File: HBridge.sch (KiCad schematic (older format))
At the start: 27 parts, among them Q1 RTQ020N03, Q2 RTQ020N03, Q3 RTQ020N03, Q4 RTQ020N03

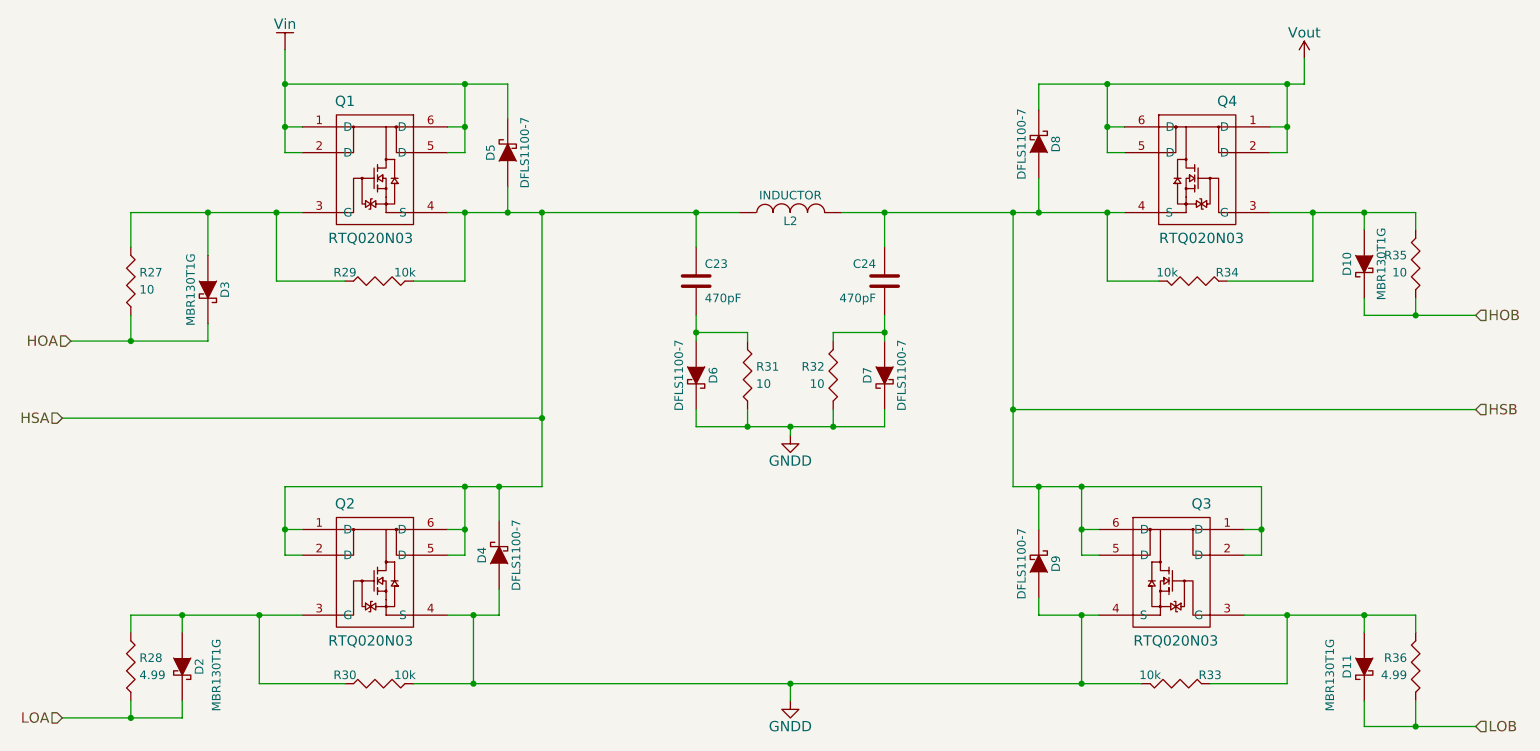
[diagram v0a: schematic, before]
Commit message: Started placing components
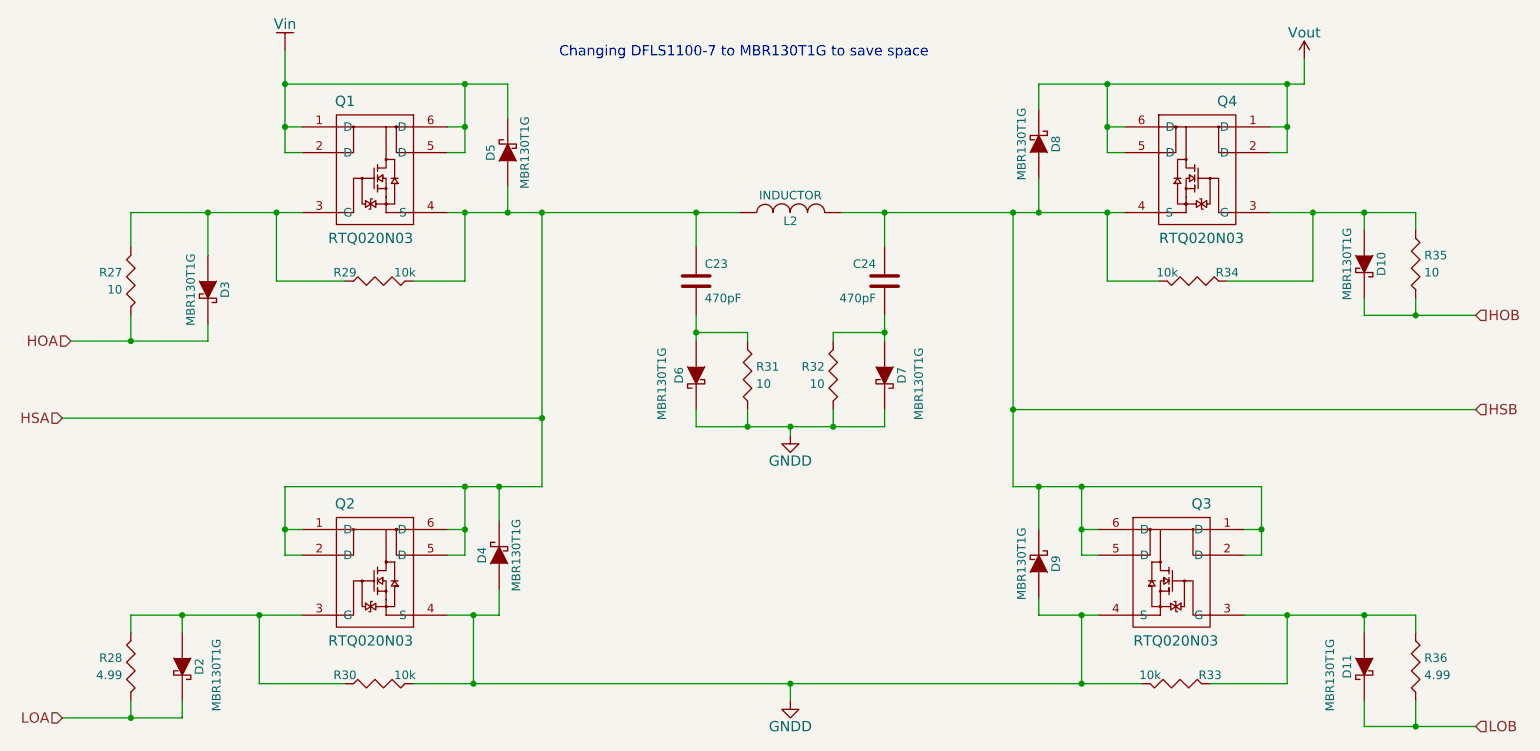
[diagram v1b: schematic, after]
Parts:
- D10, D11, D2, D3: footprint Diodes_SMD:Diode-SMA_Handsoldering -> KiCadFP:Diode-SOD_123_Handsoldering
- D4, D5, D6, D7, D8, D9: value DFLS1100-7 -> MBR130T1G; footprint Diodes_SMD:Diode-SMA_Handsoldering -> KiCadFP:Diode-SOD_123_Handsoldering; PN DFLS1100-7 -> MBR130T1G
- Q1, Q2, Q3, Q4: footprint Housings_SOT-23_SOT-143_TSOT-6:SOT23-6 -> Housings_SOT-23_SOT-143_TSOT-6:TSOT-6-MK06A_Handsoldering
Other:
- note added: "Changing DFLS1100-7 to MBR130T1G to save space"
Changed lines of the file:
@@
 LIBS:valves
 LIBS:SelfGenerated
+LIBS:ipc-7351-diode
 LIBS:Project_2-cache
 EELAYER 25 0
@@
 F 0 "Q1" V 3300 1550 60  0000 C CNN
 F 1 "RTQ020N03" V 4100 1700 60  0000 C CNN
-F 2 "Housings_SOT-23_SOT-143_TSOT-6:SOT23-6" H 3700 1750 60  0001 C CNN
+F 2 "Housings_SOT-23_SOT-143_TSOT-6:TSOT-6-MK06A_Handsoldering" H 3700 1750 60  0001 C CNN
 F 3 "" H 3700 1750 60  0000 C CNN
 	1    3700 1750
@@
 $EndComp
 $Comp
-L Vin #PWR053
+L Vin #PWR051
 U 1 1 54F15F11
 P 3150 1050
-F 0 "#PWR053" H 3150 900 60  0001 C CNN
+F 0 "#PWR051" H 3150 900 60  0001 C CNN
 F 1 "Vin" H 3150 1200 60  0000 C CNN
 F 2 "" H 3150 1050 60  0000 C CNN
@@
 F 3 "" H 2250 2400 30  0000 C CNN
 	1    2250 2400
-	1    0    0    -1
+	-1   0    0    -1
 $EndComp
 $Comp
@@
 F 0 "D3" H 2700 2550 50  0000 C CNN
 F 1 "MBR130T1G" H 2700 2350 50  0000 C CNN
-F 2 "Diodes_SMD:Diode-SMA_Handsoldering" H 2700 2450 60  0001 C CNN
+F 2 "KiCadFP:Diode-SOD_123_Handsoldering" H 2700 2450 60  0001 C CNN
 F 3 "" H 2700 2450 60  0000 C CNN
 F 4 "MBR130T1G" H 2700 2450 60  0001 C CNN "PN"
@@
 $EndComp
 $Comp
-L DIODESCH D5
-U 1 1 54F16C43
-P 4450 1650
-F 0 "D5" H 4450 1750 50  0000 C CNN
-F 1 "DFLS1100-7" H 4450 1550 50  0000 C CNN
-F 2 "Diodes_SMD:Diode-SMA_Handsoldering" H 4450 1650 60  0001 C CNN
-F 3 "" H 4450 1650 60  0000 C CNN
-F 4 "DFLS1100-7" H 4450 1650 60  0001 C CNN "PN"
-	1    4450 1650
-	0    -1   -1   0
-$EndComp
-$Comp
 L Rv R28
 U 1 1 54F17237
@@
 F 3 "" H 2250 4650 30  0000 C CNN
 	1    2250 4650
-	1    0    0    -1
+	-1   0    0    -1
 $EndComp
 $Comp
@@
 F 0 "D2" H 2550 4750 50  0000 C CNN
 F 1 "MBR130T1G" H 2600 4850 50  0000 C CNN
-F 2 "Diodes_SMD:Diode-SMA_Handsoldering" H 2550 4650 60  0001 C CNN
+F 2 "KiCadFP:Diode-SOD_123_Handsoldering" H 2550 4650 60  0001 C CNN
 F 3 "" H 2550 4650 60  0000 C CNN
 F 4 "MBR130T1G" H 2550 4650 60  0001 C CNN "PN"
@@
 F 0 "Q2" V 3300 3900 60  0000 C CNN
 F 1 "RTQ020N03" V 4100 4050 60  0000 C CNN
-F 2 "Housings_SOT-23_SOT-143_TSOT-6:SOT23-6" H 3700 4100 60  0001 C CNN
+F 2 "Housings_SOT-23_SOT-143_TSOT-6:TSOT-6-MK06A_Handsoldering" H 3700 4100 60  0001 C CNN
 F 3 "" H 3700 4100 60  0000 C CNN
 	1    3700 4100
 	0    1    1    0
-$EndComp
-$Comp
-L DIODESCH D4
-U 1 1 54F1760B
-P 4400 4000
-F 0 "D4" H 4400 4100 50  0000 C CNN
-F 1 "DFLS1100-7" H 4400 3900 50  0000 C CNN
-F 2 "Diodes_SMD:Diode-SMA_Handsoldering" H 4400 4000 60  0001 C CNN
-F 3 "" H 4400 4000 60  0000 C CNN
-F 4 "DFLS1100-7" H 4400 4000 60  0001 C CNN "PN"
-	1    4400 4000
-	0    -1   -1   0
 $EndComp
 $Comp
@@
 $EndComp
 $Comp
-L DIODESCH D6
-U 1 1 54F1B1EB
-P 5550 2950
-F 0 "D6" H 5550 3050 50  0000 C CNN
-F 1 "DFLS1100-7" H 5550 2850 50  0000 C CNN
-F 2 "Diodes_SMD:Diode-SMA_Handsoldering" H 5550 2950 60  0001 C CNN
-F 3 "" H 5550 2950 60  0000 C CNN
-F 4 "DFLS1100-7" H 5550 2950 60  0001 C CNN "PN"
-	1    5550 2950
-	0    1    1    0
-$EndComp
-$Comp
 L Rv R31
 U 1 1 54F1B288
@@
 F 0 "Q4" V 8050 1550 60  0000 C CNN
 F 1 "RTQ020N03" V 8850 1700 60  0000 C CNN
-F 2 "Housings_SOT-23_SOT-143_TSOT-6:SOT23-6" H 8450 1750 60  0001 C CNN
+F 2 "Housings_SOT-23_SOT-143_TSOT-6:TSOT-6-MK06A_Handsoldering" H 8450 1750 60  0001 C CNN
 F 3 "" H 8450 1750 60  0000 C CNN
 	1    8450 1750
@@
 F 3 "" H 9750 2300 30  0000 C CNN
 	1    9750 2300
-	-1   0    0    -1
+	1    0    0    -1
 $EndComp
 $Comp
@@
 F 0 "D10" H 9450 2400 50  0000 C CNN
 F 1 "MBR130T1G" H 9450 2200 50  0000 C CNN
-F 2 "Diodes_SMD:Diode-SMA_Handsoldering" H 9450 2300 60  0001 C CNN
+F 2 "KiCadFP:Diode-SOD_123_Handsoldering" H 9450 2300 60  0001 C CNN
 F 3 "" H 9450 2300 60  0000 C CNN
 F 4 "MBR130T1G" H 9450 2300 60  0001 C CNN "PN"
 	1    9450 2300
-	0    -1   1    0
+	0    1    1    0
 $EndComp
 $Comp
@@
 $EndComp
 $Comp
-L DIODESCH D8
-U 1 1 54F1CF31
-P 7550 1600
-F 0 "D8" H 7550 1700 50  0000 C CNN
-F 1 "DFLS1100-7" H 7550 1500 50  0000 C CNN
-F 2 "Diodes_SMD:Diode-SMA_Handsoldering" H 7550 1600 60  0001 C CNN
-F 3 "" H 7550 1600 60  0000 C CNN
-F 4 "DFLS1100-7" H 7550 1600 60  0001 C CNN "PN"
-	1    7550 1600
-	0    1    -1   0
-$EndComp
-$Comp
 L Rv R36
 U 1 1 54F1CF37
@@
 F 3 "" H 9750 4650 30  0000 C CNN
 	1    9750 4650
-	-1   0    0    -1
+	1    0    0    -1
 $EndComp
 $Comp
@@
 F 0 "D11" H 9450 4750 50  0000 C CNN
 F 1 "MBR130T1G" H 9500 4850 50  0000 C CNN
-F 2 "Diodes_SMD:Diode-SMA_Handsoldering" H 9450 4650 60  0001 C CNN
+F 2 "KiCadFP:Diode-SOD_123_Handsoldering" H 9450 4650 60  0001 C CNN
 F 3 "" H 9450 4650 60  0000 C CNN
 F 4 "MBR130T1G" H 9450 4650 60  0001 C CNN "PN"
@@
 F 0 "Q3" V 7900 3900 60  0000 C CNN
 F 1 "RTQ020N03" V 8700 4050 60  0000 C CNN
-F 2 "Housings_SOT-23_SOT-143_TSOT-6:SOT23-6" H 8300 4100 60  0001 C CNN
+F 2 "Housings_SOT-23_SOT-143_TSOT-6:TSOT-6-MK06A_Handsoldering" H 8300 4100 60  0001 C CNN
 F 3 "" H 8300 4100 60  0000 C CNN
 	1    8300 4100
 	0    -1   1    0
-$EndComp
-$Comp
-L DIODESCH D9
-U 1 1 54F1CF4B
-P 7550 4050
-F 0 "D9" H 7550 4150 50  0000 C CNN
-F 1 "DFLS1100-7" H 7550 3950 50  0000 C CNN
-F 2 "Diodes_SMD:Diode-SMA_Handsoldering" H 7550 4050 60  0001 C CNN
-F 3 "" H 7550 4050 60  0000 C CNN
-F 4 "DFLS1100-7" H 7550 4050 60  0001 C CNN "PN"
-	1    7550 4050
-	0    1    -1   0
 $EndComp
 $Comp
@@
 $EndComp
 $Comp
-L DIODESCH D7
-U 1 1 54F1CF91
-P 6650 2950
-F 0 "D7" H 6650 3050 50  0000 C CNN
-F 1 "DFLS1100-7" H 6650 2850 50  0000 C CNN
-F 2 "Diodes_SMD:Diode-SMA_Handsoldering" H 6650 2950 60  0001 C CNN
-F 3 "" H 6650 2950 60  0000 C CNN
-F 4 "DFLS1100-7" H 6650 2950 60  0001 C CNN "PN"
-	1    6650 2950
-	0    -1   1    0
-$EndComp
-$Comp
 L Rv R32
 U 1 1 54F1CF97
@@
 $EndComp
 $Comp
-L GNDD #PWR054
+L GNDD #PWR052
 U 1 1 54F229CA
 P 6100 3300
-F 0 "#PWR054" H 6100 3050 60  0001 C CNN
+F 0 "#PWR052" H 6100 3050 60  0001 C CNN
 F 1 "GNDD" H 6100 3150 60  0000 C CNN
 F 2 "" H 6100 3300 60  0000 C CNN
@@
 $EndComp
 $Comp
-L Vout #PWR055
+L Vout #PWR053
 U 1 1 54F24EF6
 P 9100 1100
-F 0 "#PWR055" H 9100 950 60  0001 C CNN
+F 0 "#PWR053" H 9100 950 60  0001 C CNN
 F 1 "Vout" H 9100 1250 60  0000 C CNN
 F 2 "" H 9100 1100 60  0000 C CNN
@@
 Connection ~ 2700 2000
 $Comp
-L GNDD #PWR056
+L GNDD #PWR054
 U 1 1 54F243ED
 P 6100 4850
-F 0 "#PWR056" H 6100 4600 60  0001 C CNN
+F 0 "#PWR054" H 6100 4600 60  0001 C CNN
 F 1 "GNDD" H 6100 4700 60  0000 C CNN
 F 2 "" H 6100 4850 60  0000 C CNN
@@
 Connection ~ 6100 4750
 Connection ~ 7800 4750
+Text Notes 4750 1100 0    60   ~ 0
+Changing DFLS1100-7 to MBR130T1G to save space
+$Comp
+L DIODESCH D5
+U 1 1 54FDD309
+P 4450 1650
+F 0 "D5" H 4450 1750 50  0000 C CNN
+F 1 "MBR130T1G" H 4450 1550 50  0000 C CNN
+F 2 "KiCadFP:Diode-SOD_123_Handsoldering" H 4450 1650 60  0001 C CNN
+F 3 "" H 4450 1650 60  0000 C CNN
+F 4 "MBR130T1G" H 4450 1650 60  0001 C CNN "PN"
+	1    4450 1650
+	0    -1   -1   0
+$EndComp
+$Comp
+L DIODESCH D8
+U 1 1 54FDD344
+P 7550 1600
+F 0 "D8" H 7550 1700 50  0000 C CNN
+F 1 "MBR130T1G" H 7550 1500 50  0000 C CNN
+F 2 "KiCadFP:Diode-SOD_123_Handsoldering" H 7550 1600 60  0001 C CNN
+F 3 "" H 7550 1600 60  0000 C CNN
+F 4 "MBR130T1G" H 7550 1600 60  0001 C CNN "PN"
+	1    7550 1600
+	0    1    -1   0
+$EndComp
+$Comp
+L DIODESCH D9
+U 1 1 54FDD383
+P 7550 4050
+F 0 "D9" H 7550 4150 50  0000 C CNN
+F 1 "MBR130T1G" H 7550 3950 50  0000 C CNN
+F 2 "KiCadFP:Diode-SOD_123_Handsoldering" H 7550 4050 60  0001 C CNN
+F 3 "" H 7550 4050 60  0000 C CNN
+F 4 "MBR130T1G" H 7550 4050 60  0001 C CNN "PN"
+	1    7550 4050
+	0    1    -1   0
+$EndComp
+$Comp
+L DIODESCH D4
+U 1 1 54FDD3C3
+P 4400 4000
+F 0 "D4" H 4400 4100 50  0000 C CNN
+F 1 "MBR130T1G" H 4400 3900 50  0000 C CNN
+F 2 "KiCadFP:Diode-SOD_123_Handsoldering" H 4400 4000 60  0001 C CNN
+F 3 "" H 4400 4000 60  0000 C CNN
+F 4 "MBR130T1G" H 4400 4000 60  0001 C CNN "PN"
+	1    4400 4000
+	0    -1   -1   0
+$EndComp
+$Comp
+L DIODESCH D6
+U 1 1 54FDD554
+P 5550 2950
+F 0 "D6" H 5550 3050 50  0000 C CNN
+F 1 "MBR130T1G" H 5600 3150 50  0000 C CNN
+F 2 "KiCadFP:Diode-SOD_123_Handsoldering" H 5550 2950 60  0001 C CNN
+F 3 "" H 5550 2950 60  0000 C CNN
+F 4 "MBR130T1G" H 5550 2950 60  0001 C CNN "PN"
+	1    5550 2950
+	0    -1   1    0
+$EndComp
+$Comp
+L DIODESCH D7
+U 1 1 54FDD587
+P 6650 2950
+F 0 "D7" H 6650 3050 50  0000 C CNN
+F 1 "MBR130T1G" H 6700 3150 50  0000 C CNN
+F 2 "KiCadFP:Diode-SOD_123_Handsoldering" H 6650 2950 60  0001 C CNN
+F 3 "" H 6650 2950 60  0000 C CNN
+F 4 "MBR130T1G" H 6650 2950 60  0001 C CNN "PN"
+	1    6650 2950
+	0    1    1    0
+$EndComp
 $EndSCHEMATC

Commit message: still trying to get initial placements done.  Still need to fine-tune
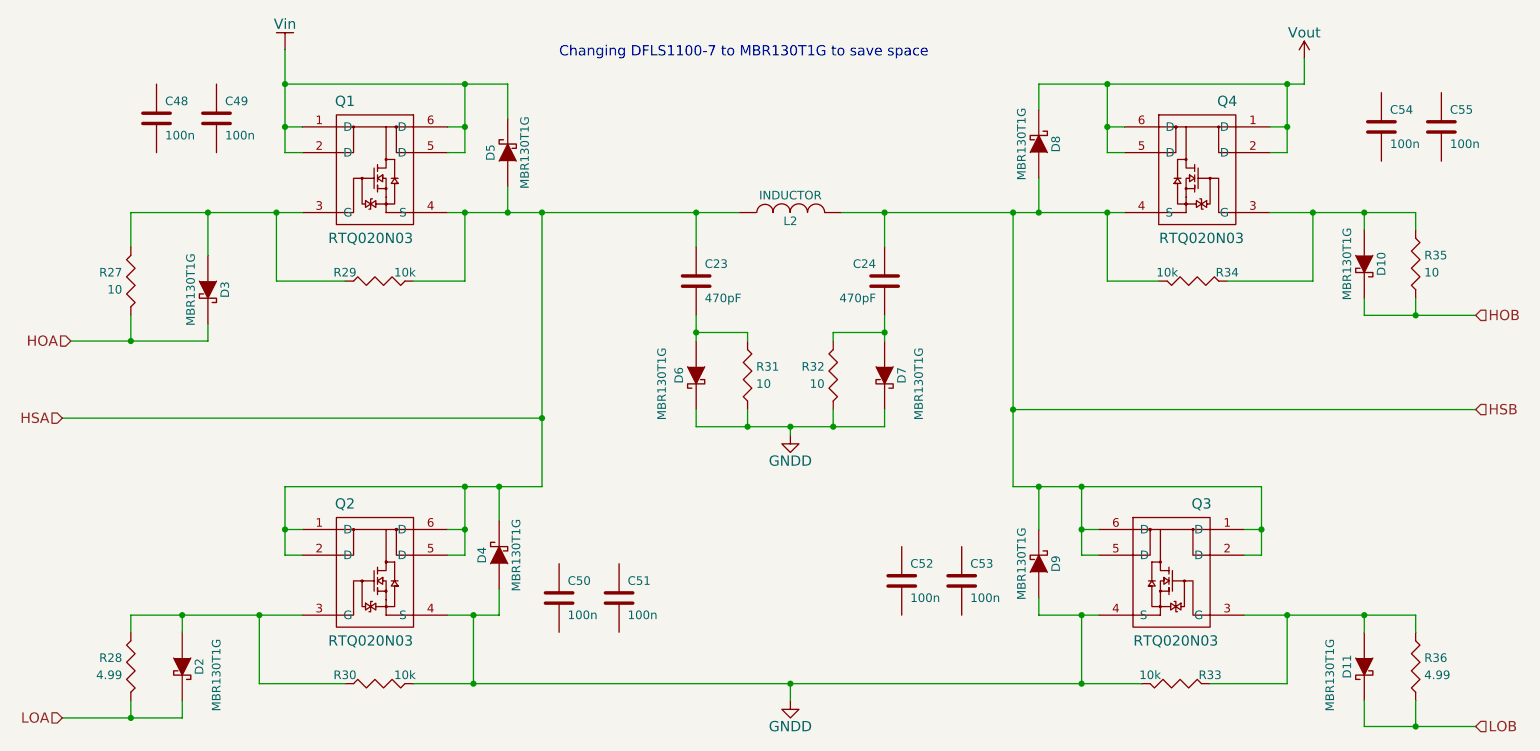
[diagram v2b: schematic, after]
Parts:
- added C48, C49, C50, C51, C52, C53, C54, C55: 100n, symbol C
- C23, C24: footprint Capacitors_SMD:C_0805_HandSoldering -> Capacitors_SMD:C_0603_HandSoldering
- R27, R28, R29, R30, R31, R32, R33, R34, R35, R36: footprint Resistors_SMD:R_0805_HandSoldering -> Resistors_SMD:R_0603_HandSoldering
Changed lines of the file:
@@
 F 0 "R27" H 2300 2450 50  0000 L CNN
 F 1 "10" H 2300 2350 50  0000 L CNN
-F 2 "Resistors_SMD:R_0805_HandSoldering" V 2180 2400 30  0001 C CNN
+F 2 "Resistors_SMD:R_0603_HandSoldering" V 2180 2400 30  0001 C CNN
 F 3 "" H 2250 2400 30  0000 C CNN
 	1    2250 2400
@@
 F 0 "R29" H 3500 2450 50  0000 C CNN
 F 1 "10k" H 3850 2450 50  0000 C CNN
-F 2 "Resistors_SMD:R_0805_HandSoldering" H 3700 2330 30  0001 C CNN
+F 2 "Resistors_SMD:R_0603_HandSoldering" H 3700 2330 30  0001 C CNN
 F 3 "" V 3700 2400 30  0000 C CNN
 	1    3700 2400
@@
 F 0 "R28" H 2300 4700 50  0000 L CNN
 F 1 "4.99" H 2300 4600 50  0000 L CNN
-F 2 "Resistors_SMD:R_0805_HandSoldering" V 2180 4650 30  0001 C CNN
+F 2 "Resistors_SMD:R_0603_HandSoldering" V 2180 4650 30  0001 C CNN
 F 3 "" H 2250 4650 30  0000 C CNN
 	1    2250 4650
@@
 F 0 "R30" H 3500 4800 50  0000 C CNN
 F 1 "10k" H 3850 4800 50  0000 C CNN
-F 2 "Resistors_SMD:R_0805_HandSoldering" H 3700 4680 30  0001 C CNN
+F 2 "Resistors_SMD:R_0603_HandSoldering" H 3700 4680 30  0001 C CNN
 F 3 "" V 3700 4750 30  0000 C CNN
 	1    3700 4750
@@
 F 0 "R31" H 5900 3000 50  0000 L CNN
 F 1 "10" H 5900 2900 50  0000 L CNN
-F 2 "Resistors_SMD:R_0805_HandSoldering" V 5780 2950 30  0001 C CNN
+F 2 "Resistors_SMD:R_0603_HandSoldering" V 5780 2950 30  0001 C CNN
 F 3 "" H 5850 2950 30  0000 C CNN
 	1    5850 2950
@@
 F 0 "C23" H 5600 2500 50  0000 L CNN
 F 1 "470pF" H 5600 2300 50  0000 L CNN
-F 2 "Capacitors_SMD:C_0805_HandSoldering" H 5588 2250 30  0001 C CNN
+F 2 "Capacitors_SMD:C_0603_HandSoldering" H 5588 2250 30  0001 C CNN
 F 3 "" H 5550 2400 60  0000 C CNN
 	1    5550 2400
@@
 F 0 "R35" H 9800 2350 50  0000 L CNN
 F 1 "10" H 9800 2250 50  0000 L CNN
-F 2 "Resistors_SMD:R_0805_HandSoldering" V 9680 2300 30  0001 C CNN
+F 2 "Resistors_SMD:R_0603_HandSoldering" V 9680 2300 30  0001 C CNN
 F 3 "" H 9750 2300 30  0000 C CNN
 	1    9750 2300
@@
 F 0 "R34" H 8250 2450 50  0000 C CNN
 F 1 "10k" H 8600 2450 50  0000 C CNN
-F 2 "Resistors_SMD:R_0805_HandSoldering" H 8450 2330 30  0001 C CNN
+F 2 "Resistors_SMD:R_0603_HandSoldering" H 8450 2330 30  0001 C CNN
 F 3 "" V 8450 2400 30  0000 C CNN
 	1    8450 2400
@@
 F 0 "R36" H 9800 4700 50  0000 L CNN
 F 1 "4.99" H 9800 4600 50  0000 L CNN
-F 2 "Resistors_SMD:R_0805_HandSoldering" V 9680 4650 30  0001 C CNN
+F 2 "Resistors_SMD:R_0603_HandSoldering" V 9680 4650 30  0001 C CNN
 F 3 "" H 9750 4650 30  0000 C CNN
 	1    9750 4650
@@
 F 0 "R33" H 8150 4800 50  0000 C CNN
 F 1 "10k" H 8500 4800 50  0000 C CNN
-F 2 "Resistors_SMD:R_0805_HandSoldering" H 8350 4680 30  0001 C CNN
+F 2 "Resistors_SMD:R_0603_HandSoldering" H 8350 4680 30  0001 C CNN
 F 3 "" V 8350 4750 30  0000 C CNN
 	1    8350 4750
@@
 F 0 "R32" H 6400 3000 50  0000 L CNN
 F 1 "10" H 6400 2900 50  0000 L CNN
-F 2 "Resistors_SMD:R_0805_HandSoldering" V 6280 2950 30  0001 C CNN
+F 2 "Resistors_SMD:R_0603_HandSoldering" V 6280 2950 30  0001 C CNN
 F 3 "" H 6350 2950 30  0000 C CNN
 	1    6350 2950
@@
 F 0 "C24" H 6700 2500 50  0000 L CNN
 F 1 "470pF" H 6700 2300 50  0000 L CNN
-F 2 "Capacitors_SMD:C_0805_HandSoldering" H 6688 2250 30  0001 C CNN
+F 2 "Capacitors_SMD:C_0603_HandSoldering" H 6688 2250 30  0001 C CNN
 F 3 "" H 6650 2400 60  0000 C CNN
 	1    6650 2400
@@
 	0    1    1    0
 $EndComp
+$Comp
+L C C48
+U 1 1 54FF5EFC
+P 2400 1450
+F 0 "C48" H 2450 1550 50  0000 L CNN
+F 1 "100n" H 2450 1350 50  0000 L CNN
+F 2 "" H 2438 1300 30  0000 C CNN
+F 3 "" H 2400 1450 60  0000 C CNN
+	1    2400 1450
+	1    0    0    -1
+$EndComp
+$Comp
+L C C49
+U 1 1 54FF5FC2
+P 2750 1450
+F 0 "C49" H 2800 1550 50  0000 L CNN
+F 1 "100n" H 2800 1350 50  0000 L CNN
+F 2 "" H 2788 1300 30  0000 C CNN
+F 3 "" H 2750 1450 60  0000 C CNN
+	1    2750 1450
+	1    0    0    -1
+$EndComp
+$Comp
+L C C50
+U 1 1 54FF60EA
+P 4750 4250
+F 0 "C50" H 4800 4350 50  0000 L CNN
+F 1 "100n" H 4800 4150 50  0000 L CNN
+F 2 "" H 4788 4100 30  0000 C CNN
+F 3 "" H 4750 4250 60  0000 C CNN
+	1    4750 4250
+	1    0    0    -1
+$EndComp
+$Comp
+L C C51
+U 1 1 54FF60F0
+P 5100 4250
+F 0 "C51" H 5150 4350 50  0000 L CNN
+F 1 "100n" H 5150 4150 50  0000 L CNN
+F 2 "" H 5138 4100 30  0000 C CNN
+F 3 "" H 5100 4250 60  0000 C CNN
+	1    5100 4250
+	1    0    0    -1
+$EndComp
+$Comp
+L C C52
+U 1 1 54FF6137
+P 6750 4150
+F 0 "C52" H 6800 4250 50  0000 L CNN
+F 1 "100n" H 6800 4050 50  0000 L CNN
+F 2 "" H 6788 4000 30  0000 C CNN
+F 3 "" H 6750 4150 60  0000 C CNN
+	1    6750 4150
+	1    0    0    -1
+$EndComp
+$Comp
+L C C53
+U 1 1 54FF613D
+P 7100 4150
+F 0 "C53" H 7150 4250 50  0000 L CNN
+F 1 "100n" H 7150 4050 50  0000 L CNN
+F 2 "" H 7138 4000 30  0000 C CNN
+F 3 "" H 7100 4150 60  0000 C CNN
+	1    7100 4150
+	1    0    0    -1
+$EndComp
+$Comp
+L C C54
+U 1 1 54FF6287
+P 9550 1500
+F 0 "C54" H 9600 1600 50  0000 L CNN
+F 1 "100n" H 9600 1400 50  0000 L CNN
+F 2 "" H 9588 1350 30  0000 C CNN
+F 3 "" H 9550 1500 60  0000 C CNN
+	1    9550 1500
+	1    0    0    -1
+$EndComp
+$Comp
+L C C55
+U 1 1 54FF628D
+P 9900 1500
+F 0 "C55" H 9950 1600 50  0000 L CNN
+F 1 "100n" H 9950 1400 50  0000 L CNN
+F 2 "" H 9938 1350 30  0000 C CNN
+F 3 "" H 9900 1500 60  0000 C CNN
+	1    9900 1500
+	1    0    0    -1
+$EndComp
 $EndSCHEMATC
